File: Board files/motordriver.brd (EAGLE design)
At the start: 31.8 x 44.5 mm, 15 parts, among them Q1 IPB034N03L, U1 VNH5019A

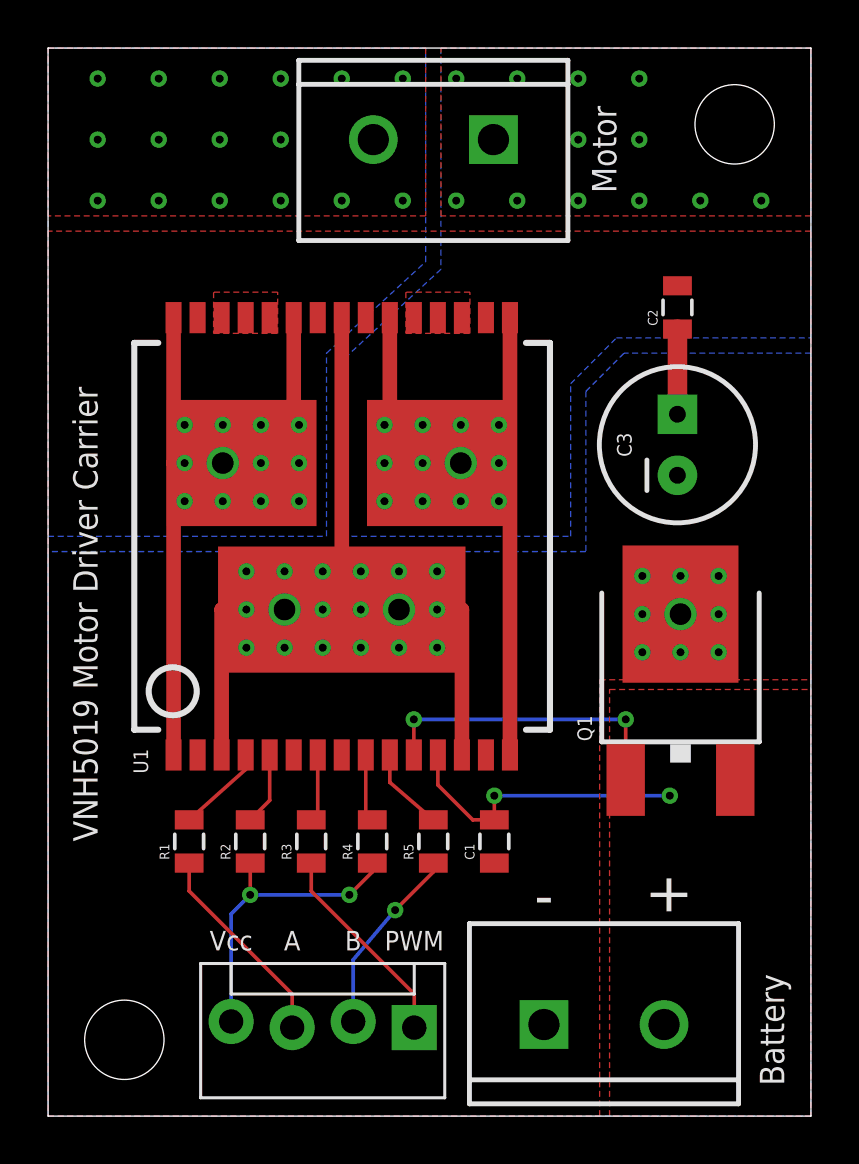
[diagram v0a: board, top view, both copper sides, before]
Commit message: Moved a capacitor
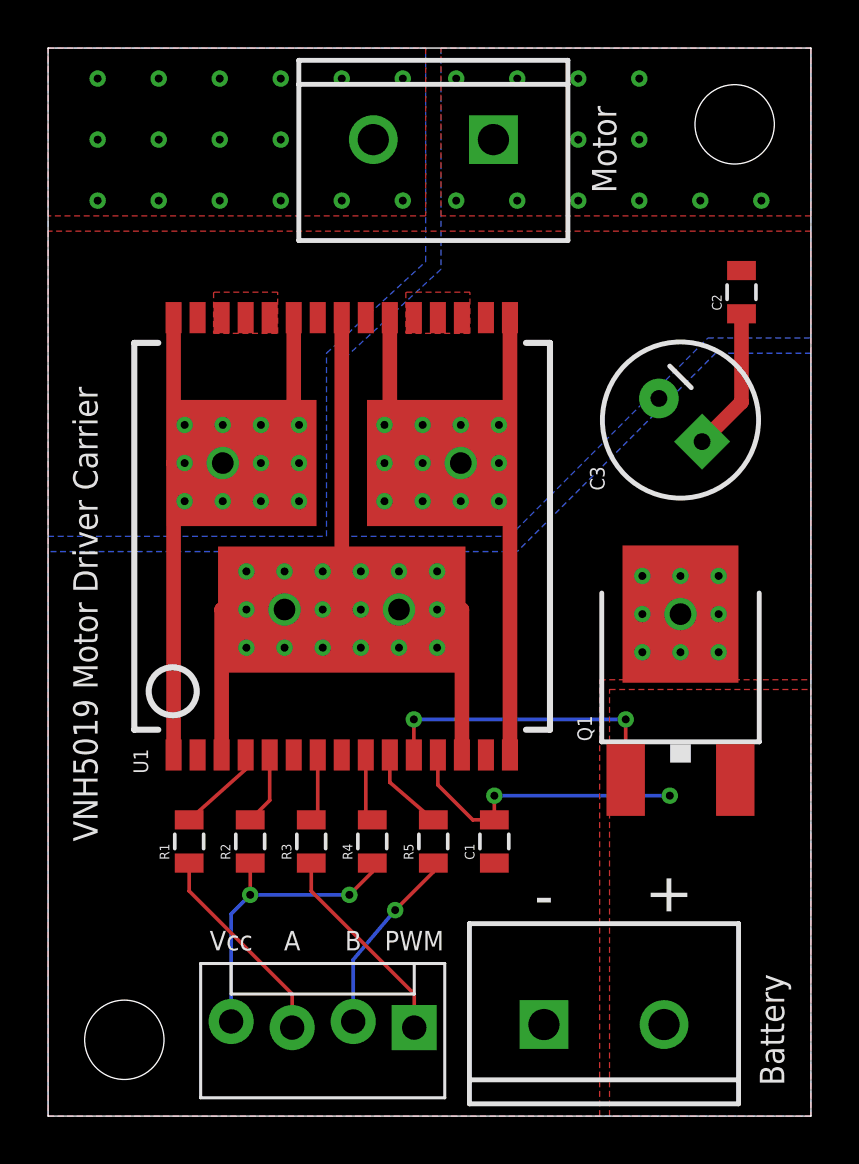
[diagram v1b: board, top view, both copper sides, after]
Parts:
- moved C2 2.74 mm to (28.9, 34.3)
- moved C3 1.04 mm to (26.3, 29.0), turned to 315 degrees
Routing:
- net VCC: track 41.3 -> 43.7 mm
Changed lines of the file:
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@@
 </element>
 <element name="C1" library="SparkFun-Capacitors" package="0805" value="0.1uF" x="18.57375" y="11.43" rot="R90"/>
-<element name="C2" library="SparkFun-Capacitors" package="0805" value="0.1uF" x="26.19375" y="33.655" rot="R90"/>
-<element name="C3" library="SparkFun-Capacitors" package="CPOL-RADIAL-100UF-25V" value="47uF" x="26.19375" y="27.94" smashed="yes" rot="R90">
-<attribute name="NAME" x="24.28875" y="27.94" size="0.6096" layer="25" rot="R90" align="bottom-center"/>
+<element name="C2" library="SparkFun-Capacitors" package="0805" value="0.1uF" x="28.86075" y="34.29" rot="R90"/>
+<element name="C3" library="SparkFun-Capacitors" package="CPOL-RADIAL-100UF-25V" value="47uF" x="26.32075" y="28.9687" smashed="yes" rot="R315">
+<attribute name="NAME" x="23.163959375" y="26.5374875" size="0.6096" layer="25" rot="R90" align="bottom-center"/>
 </element>
 <element name="R1" library="SparkFun-Resistors" package="0805" value="1k" x="5.87375" y="11.43" rot="R90"/>
@@
 <polygon width="0.254" layer="16">
 <vertex x="12.22375" y="24.13"/>
-<vertex x="21.74875" y="24.13"/>
-<vertex x="21.74875" y="30.48"/>
-<vertex x="23.65375" y="32.385"/>
+<vertex x="19.20875" y="24.13"/>
+<vertex x="27.46375" y="32.385"/>
 <vertex x="31.75" y="32.385"/>
 <vertex x="31.75" y="44.45"/>
@@
 <vertex x="31.75" y="0"/>
 <vertex x="31.75" y="31.75"/>
-<vertex x="23.97125" y="31.75"/>
-<vertex x="22.38375" y="30.1625"/>
-<vertex x="22.38375" y="23.495"/>
+<vertex x="27.78125" y="31.75"/>
+<vertex x="19.52625" y="23.495"/>
 <vertex x="0" y="23.495"/>
 </polygon>
@@
 <wire x1="26.82875" y1="20.32" x2="26.82875" y2="20.892" width="0.1524" layer="1"/>
 <wire x1="26.82875" y1="20.892" x2="26.32075" y2="20.892" width="0.1524" layer="1"/>
-<wire x1="26.19375" y1="32.755" x2="26.19375" y2="29.21" width="0.8128" layer="1"/>
+<wire x1="28.86075" y1="33.39" x2="28.86075" y2="29.712646875" width="0.6096" layer="1"/>
+<wire x1="28.86075" y1="29.712646875" x2="27.218775" y2="28.070671875" width="0.6096" layer="1"/>
 </signal>
 <signal name="3.3V">
